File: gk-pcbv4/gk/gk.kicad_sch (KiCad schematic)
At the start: 11 parts

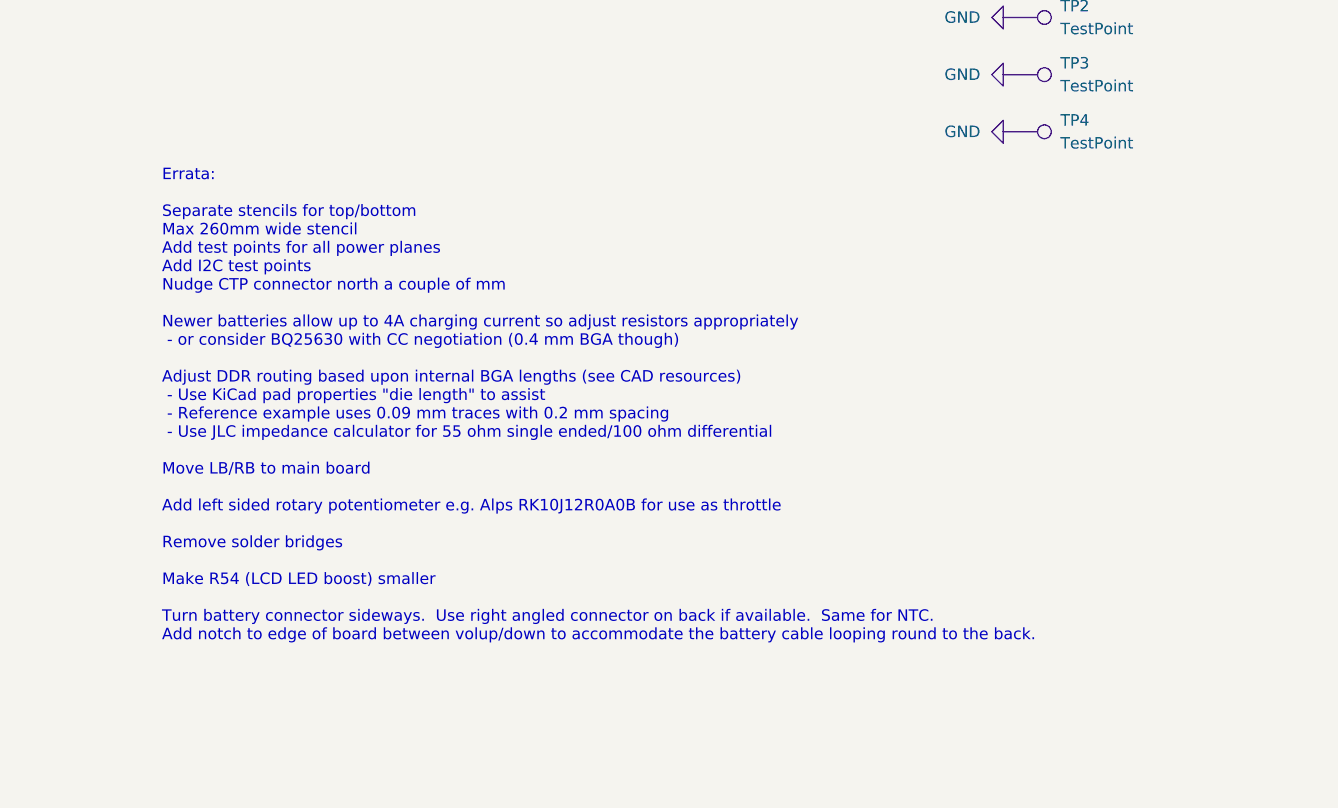
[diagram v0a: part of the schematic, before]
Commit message: remove solder bridges
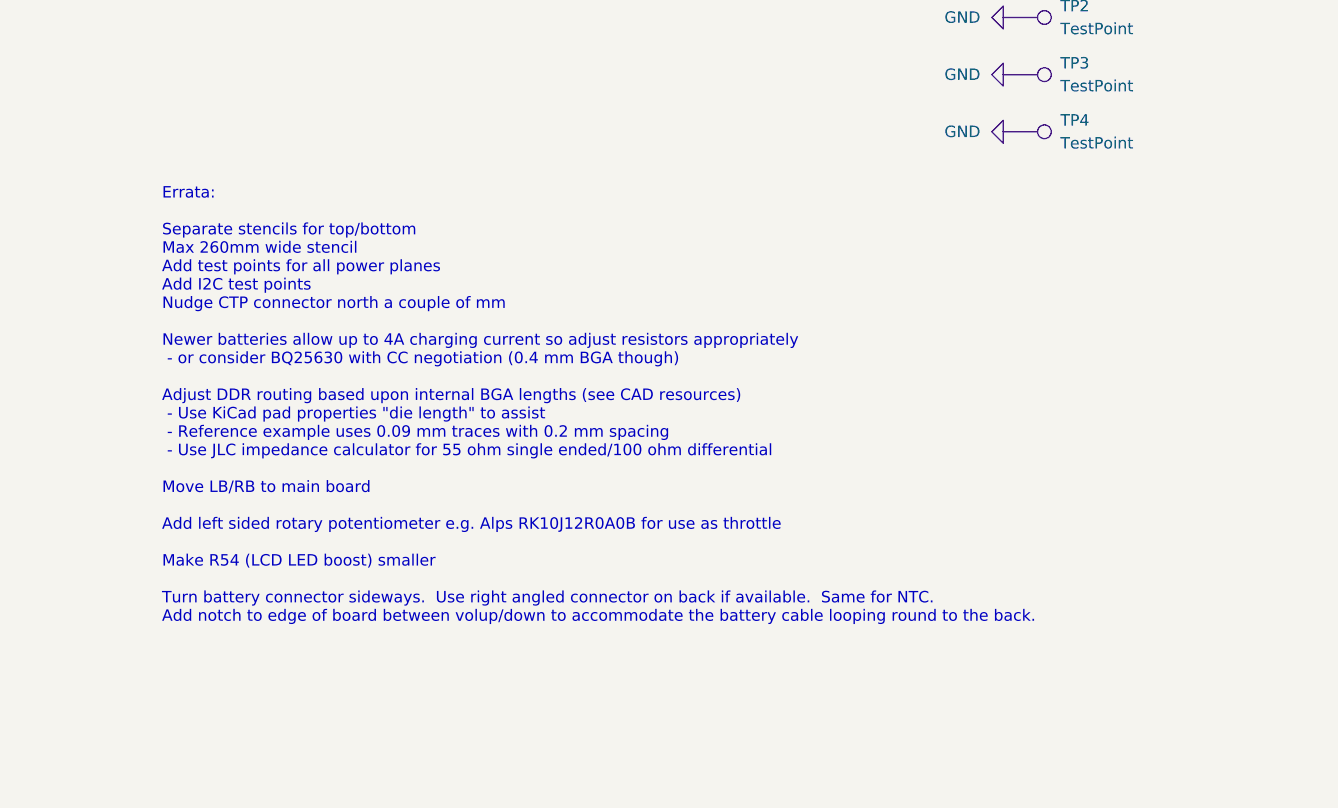
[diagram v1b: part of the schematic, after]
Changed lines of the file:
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@@
 		)
 	)
-	(text "Errata:\n\nSeparate stencils for top/bottom\nMax 260mm wide stencil\nAdd test points for all power planes\nAdd I2C test points\nNudge CTP connector north a couple of mm\n\nNewer batteries allow up to 4A charging current so adjust resistors appropriately\n - or consider BQ25630 with CC negotiation (0.4 mm BGA though)\n\nAdjust DDR routing based upon internal BGA lengths (see CAD resources)\n - Use KiCad pad properties \"die length\" to assist\n - Reference example uses 0.09 mm traces with 0.2 mm spacing\n - Use JLC impedance calculator for 55 ohm single ended/100 ohm differential\n\nMove LB/RB to main board\n\nAdd left sided rotary potentiometer e.g. Alps RK10J12R0A0B for use as throttle\n\nRemove solder bridges\n\nMake R54 (LCD LED boost) smaller\n\nTurn battery connector sideways.  Use right angled connector on back if available.  Same for NTC.\nAdd notch to edge of board between volup/down to accommodate the battery cable looping round to the back.\n"
+	(text "Errata:\n\nSeparate stencils for top/bottom\nMax 260mm wide stencil\nAdd test points for all power planes\nAdd I2C test points\nNudge CTP connector north a couple of mm\n\nNewer batteries allow up to 4A charging current so adjust resistors appropriately\n - or consider BQ25630 with CC negotiation (0.4 mm BGA though)\n\nAdjust DDR routing based upon internal BGA lengths (see CAD resources)\n - Use KiCad pad properties \"die length\" to assist\n - Reference example uses 0.09 mm traces with 0.2 mm spacing\n - Use JLC impedance calculator for 55 ohm single ended/100 ohm differential\n\nMove LB/RB to main board\n\nAdd left sided rotary potentiometer e.g. Alps RK10J12R0A0B for use as throttle\n\nMake R54 (LCD LED boost) smaller\n\nTurn battery connector sideways.  Use right angled connector on back if available.  Same for NTC.\nAdd notch to edge of board between volup/down to accommodate the battery cable looping round to the back.\n"
 		(exclude_from_sim no)
 		(at 104.648 80.01 0)

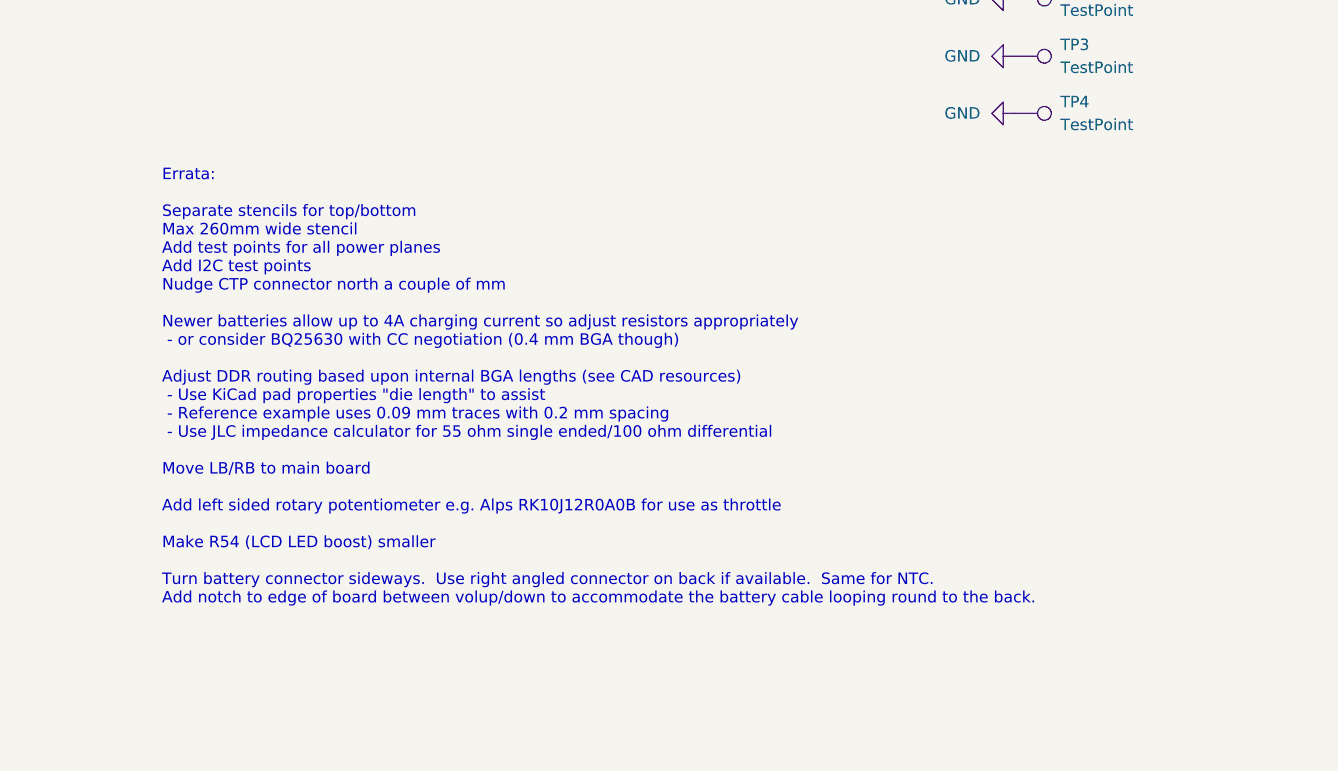
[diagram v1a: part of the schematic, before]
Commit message: turn back battery connectors sideways add notch for battery cables looping round from front
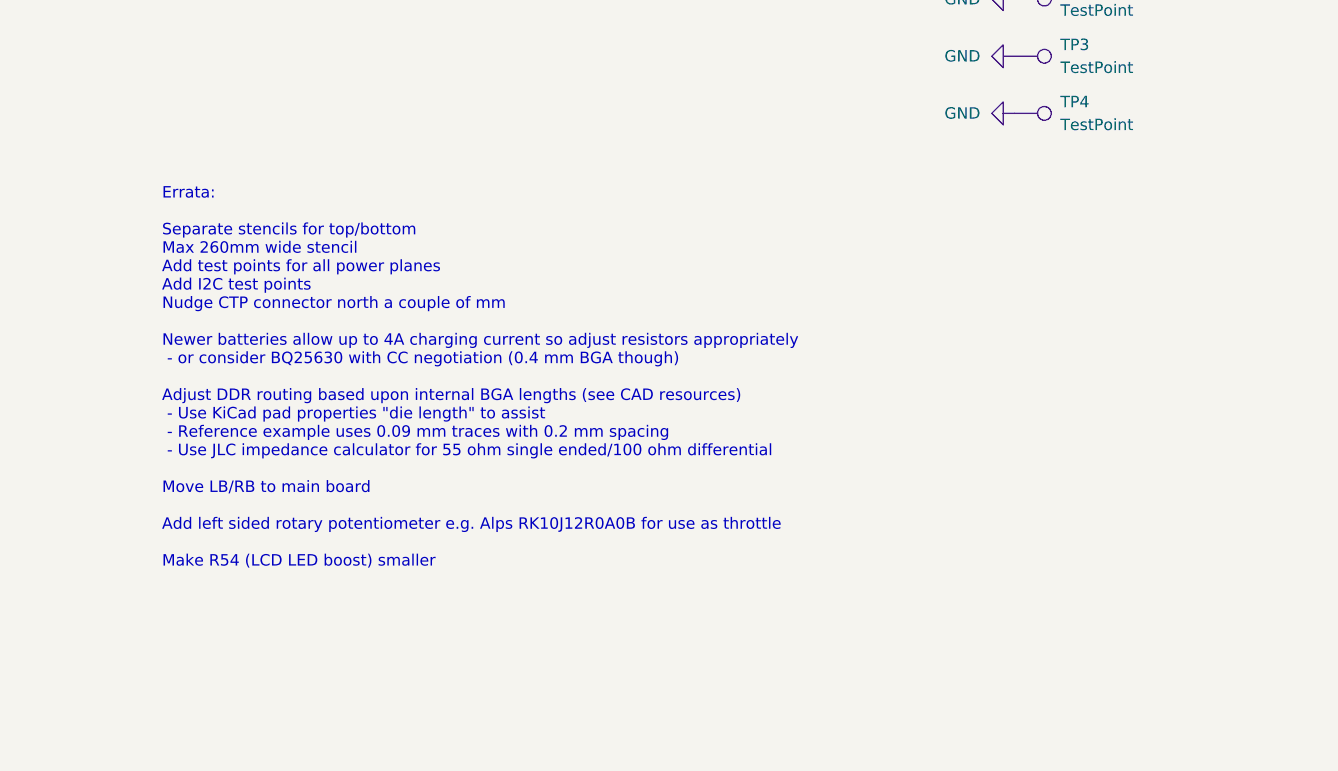
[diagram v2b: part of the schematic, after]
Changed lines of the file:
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@@
 		)
 	)
-	(text "Errata:\n\nSeparate stencils for top/bottom\nMax 260mm wide stencil\nAdd test points for all power planes\nAdd I2C test points\nNudge CTP connector north a couple of mm\n\nNewer batteries allow up to 4A charging current so adjust resistors appropriately\n - or consider BQ25630 with CC negotiation (0.4 mm BGA though)\n\nAdjust DDR routing based upon internal BGA lengths (see CAD resources)\n - Use KiCad pad properties \"die length\" to assist\n - Reference example uses 0.09 mm traces with 0.2 mm spacing\n - Use JLC impedance calculator for 55 ohm single ended/100 ohm differential\n\nMove LB/RB to main board\n\nAdd left sided rotary potentiometer e.g. Alps RK10J12R0A0B for use as throttle\n\nMake R54 (LCD LED boost) smaller\n\nTurn battery connector sideways.  Use right angled connector on back if available.  Same for NTC.\nAdd notch to edge of board between volup/down to accommodate the battery cable looping round to the back.\n"
+	(text "Errata:\n\nSeparate stencils for top/bottom\nMax 260mm wide stencil\nAdd test points for all power planes\nAdd I2C test points\nNudge CTP connector north a couple of mm\n\nNewer batteries allow up to 4A charging current so adjust resistors appropriately\n - or consider BQ25630 with CC negotiation (0.4 mm BGA though)\n\nAdjust DDR routing based upon internal BGA lengths (see CAD resources)\n - Use KiCad pad properties \"die length\" to assist\n - Reference example uses 0.09 mm traces with 0.2 mm spacing\n - Use JLC impedance calculator for 55 ohm single ended/100 ohm differential\n\nMove LB/RB to main board\n\nAdd left sided rotary potentiometer e.g. Alps RK10J12R0A0B for use as throttle\n\nMake R54 (LCD LED boost) smaller\n\n"
 		(exclude_from_sim no)
 		(at 104.648 80.01 0)

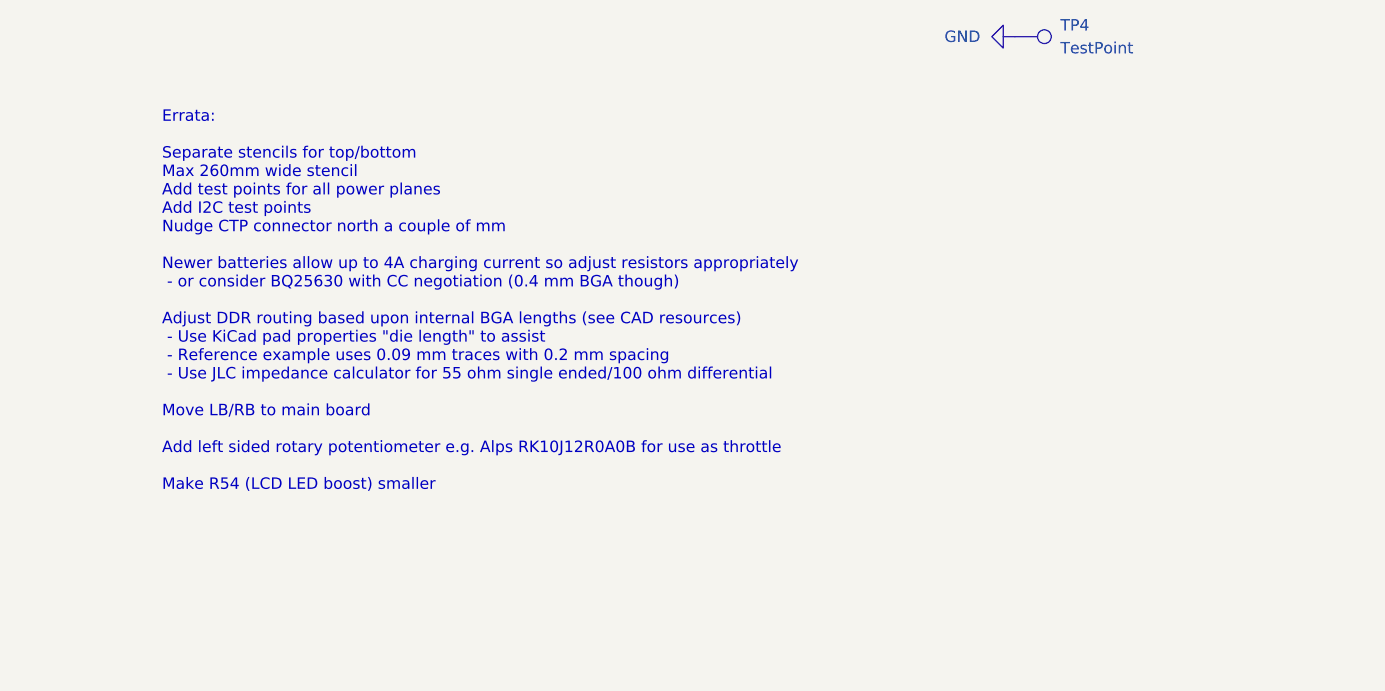
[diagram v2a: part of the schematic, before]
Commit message: add i2c test points
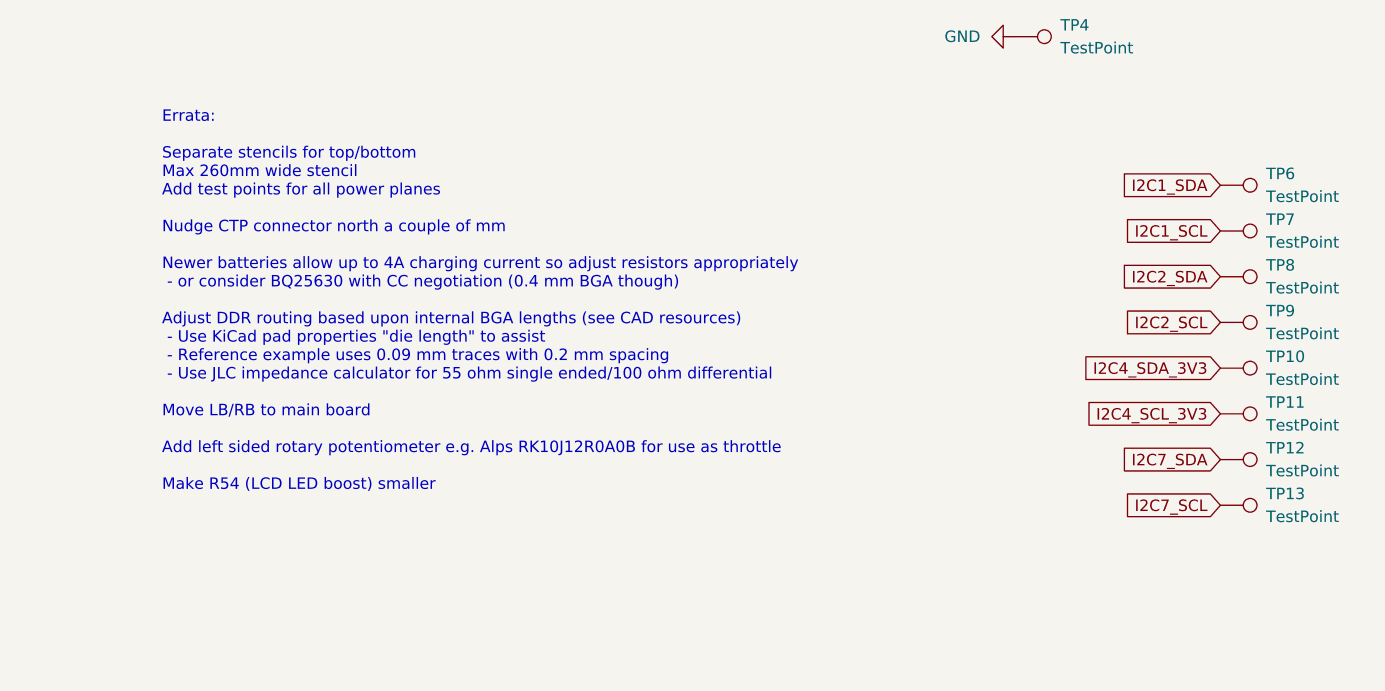
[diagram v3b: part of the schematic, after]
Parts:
- added TP10, TP11, TP12, TP13, TP6, TP7, TP8, TP9: TestPoint, Connector_PinHeader_2.54mm:PinHeader_1x01_P2.54mm_Vertical, symbol Connector:TestPoint
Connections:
- new net I2C1_SCL: TP7.1
- new net I2C1_SDA: TP6.1
- new net I2C2_SCL: TP9.1
- new net I2C2_SDA: TP8.1
- new net I2C4_SCL_3V3: TP11.1
- new net I2C4_SDA_3V3: TP10.1
- new net I2C7_SCL: TP13.1
- new net I2C7_SDA: TP12.1
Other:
- note added: "Errata: Separate stencils for top/bottom Max 260mm wide stencil Add test points for all power planes Nudge CTP connector north a couple of mm Newer batteries allow up to 4A charging current so adjust resistors appropriately - or consider BQ25630 with CC negotiation (0.4 mm BGA though) Adjust DDR routing based upon internal BGA lengths (see CAD resources) - Use KiCad pad properties "die length" to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"
- note removed: "Errata: Separate stencils for top/bottom Max 260mm wide stencil Add test points for all power planes Add I2C test points Nudge CTP connector north a couple of mm Newer batteries allow up to 4A charging current so adjust resistors appropriately - or consider BQ25630 with CC negotiation (0.4 mm BGA though) Adjust DDR routing based upon internal BGA lengths (see CAD resources) - Use KiCad pad proper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"
